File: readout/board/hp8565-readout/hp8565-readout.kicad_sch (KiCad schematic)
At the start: 18 parts, among them J1 Pin_Header, J2 Pin_Header, J3 DIP Socket, J4 Pin_Header, J5 Masach_MS230-20S, P1 DIP Pins, U1 ATmega4809-M, U2 GD75232DB

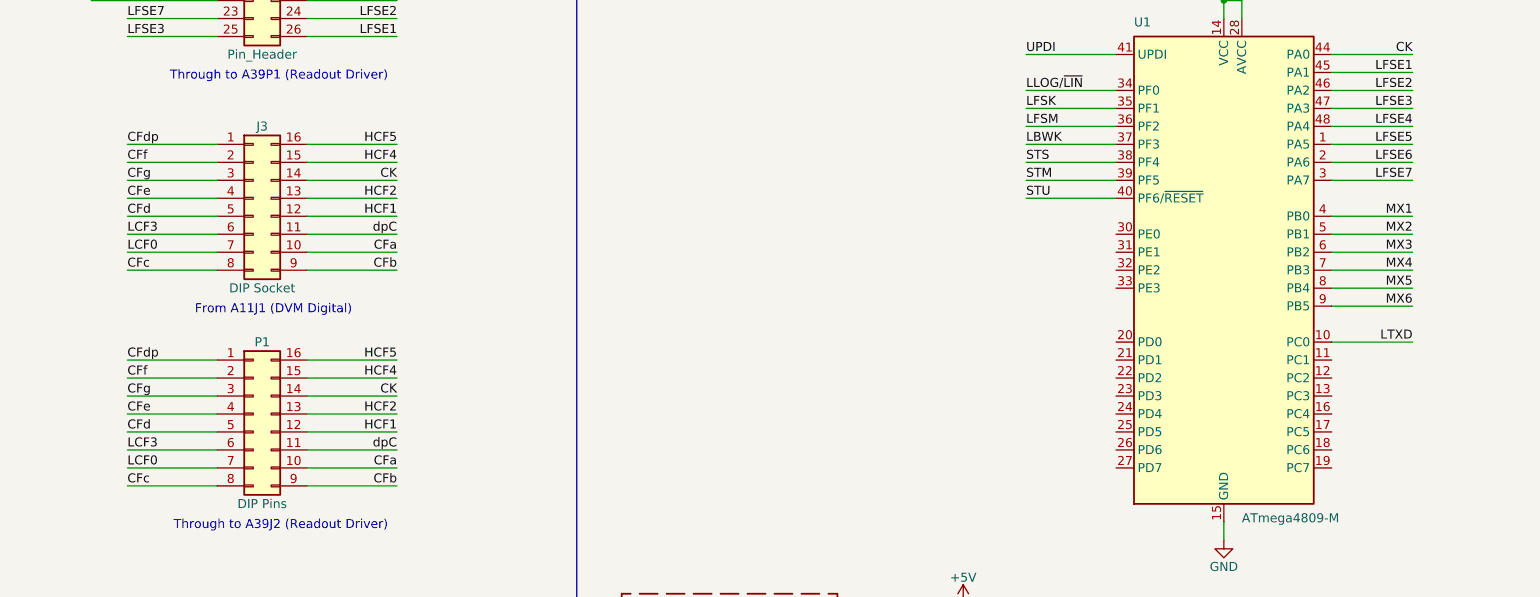
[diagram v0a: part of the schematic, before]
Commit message: Route CF connector.
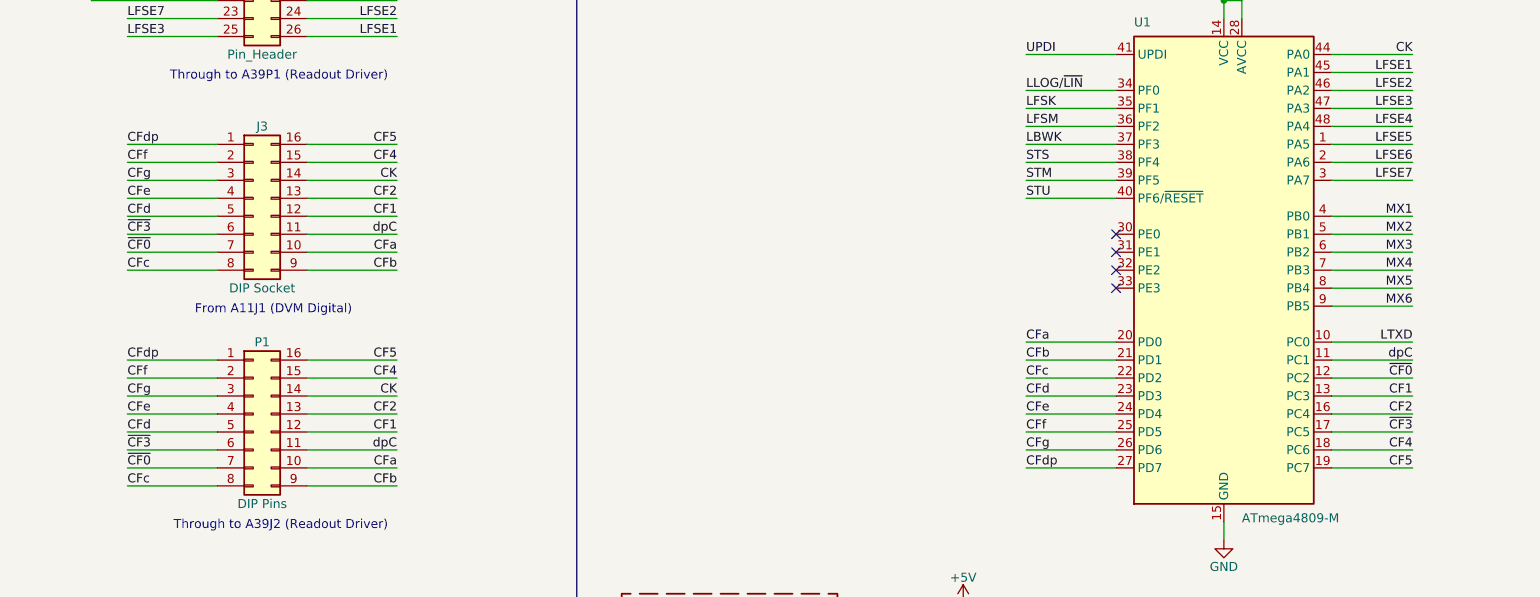
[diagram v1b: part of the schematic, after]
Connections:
- net HCF1 is gone; now on net CF1: J3.12 (Pin_12), P1.12 (Pin_12)
- net HCF2 is gone; now on net CF2: J3.13 (Pin_13), P1.13 (Pin_13)
- net HCF4 is gone; now on net CF4: J3.15 (Pin_15), P1.15 (Pin_15)
- net HCF5 is gone; now on net CF5: J3.16 (Pin_16), P1.16 (Pin_16)
- net LCF0 is gone; now on net ~{CF0}: J3.7 (Pin_7), P1.7 (Pin_7)
- net LCF3 is gone; now on net ~{CF3}: J3.6 (Pin_6), P1.6 (Pin_6)
- net CFa: now also U1.20 (PD0)
- net CFb: now also U1.21 (PD1)
- net CFc: now also U1.22 (PD2)
- net CFd: now also U1.23 (PD3)
- net CFdp: now also U1.27 (PD7)
- net CFe: now also U1.24 (PD4)
- net CFf: now also U1.25 (PD5)
- net CFg: now also U1.26 (PD6)
- net dpC: now also U1.11 (PC1)
- net ~{CF0}: now reaches U1.12 (PC2)
- net CF1: now reaches U1.13 (PC3)
- net CF2: now reaches U1.16 (PC4)
- net ~{CF3}: now reaches U1.17 (PC5)
- net CF4: now reaches U1.18 (PC6)
- net CF5: now reaches U1.19 (PC7)
- no-connect marks 3 -> 7

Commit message: Clean up silkscreen and stuff.
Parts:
- added R1: 1k5, Resistor_SMD:R_0402_1005Metric, symbol Device:R
- renumbered R1 to R5
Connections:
- net GND: now also R1.1
- net LOG/~{LIN}: now also R1.2
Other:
- moved on the sheet: R2, R3, R4, R5
